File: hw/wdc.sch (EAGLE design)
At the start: 14 parts

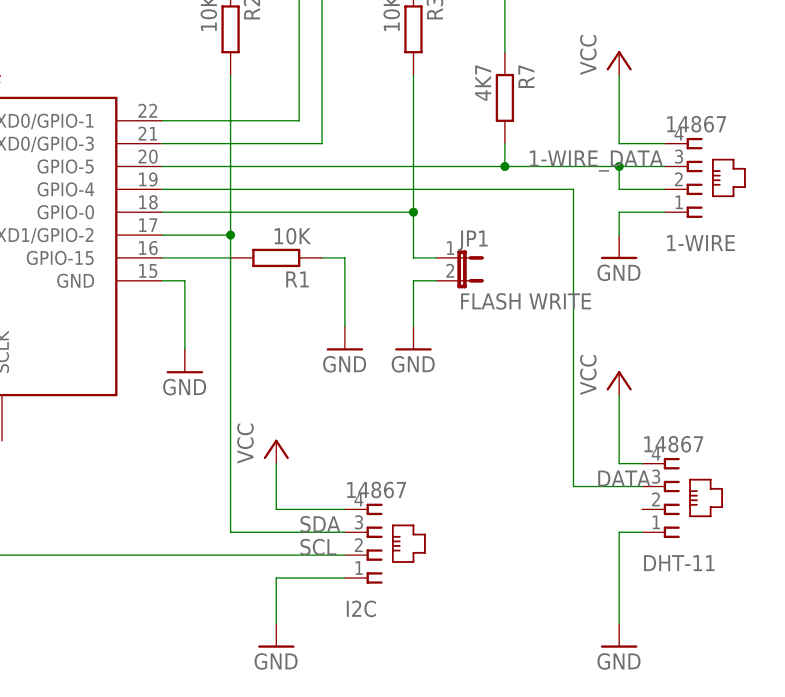
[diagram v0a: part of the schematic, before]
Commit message: Add natsCmd.js to send commands to the sensors through NATS Add wds.js to subscribe and log messages sent by the sensors through NATS Set temp sensor resolution during startup Change NATS server config to point nano pi neo
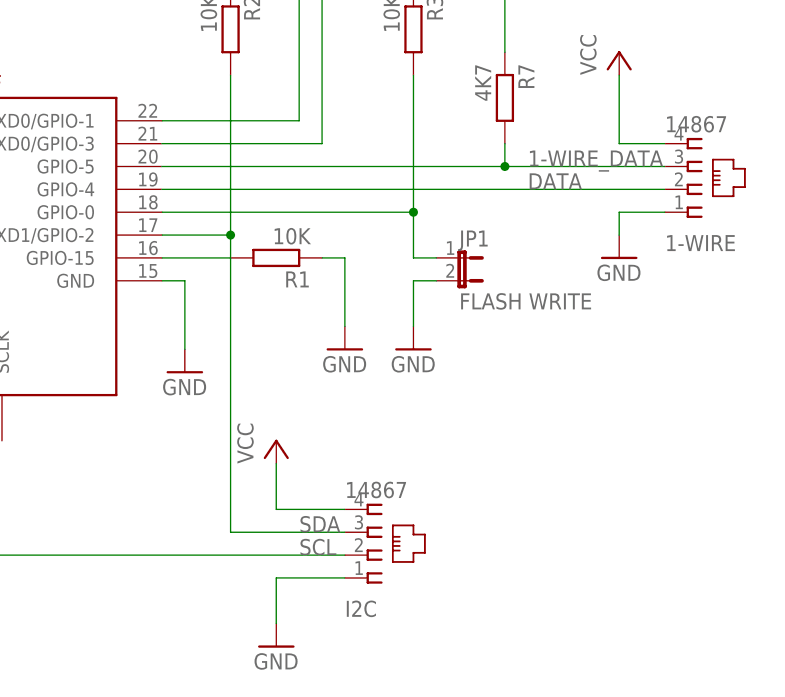
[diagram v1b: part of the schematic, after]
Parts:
- removed DHT-11: 14867, con-4ucon:14867
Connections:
- net 1-WIRE_DATA: no longer 1-WIRE.2
- net DATA: now also 1-WIRE.2; no longer DHT-11.3
- net GND: no longer DHT-11.1
- net VCC: no longer DHT-11.4
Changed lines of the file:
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@@
 <part name="GND5" library="supply1" deviceset="GND" device=""/>
 <part name="P+6" library="supply1" deviceset="VCC" device=""/>
-<part name="P+7" library="supply1" deviceset="VCC" device=""/>
-<part name="GND6" library="supply1" deviceset="GND" device=""/>
 <part name="GND7" library="supply1" deviceset="GND" device=""/>
 <part name="P+8" library="supply1" deviceset="VCC" device=""/>
@@
 <part name="GND13" library="supply1" deviceset="GND" device=""/>
 <part name="1-WIRE" library="con-4ucon" deviceset="14867" device=""/>
-<part name="DHT-11" library="con-4ucon" deviceset="14867" device=""/>
 <part name="I2C" library="con-4ucon" deviceset="14867" device=""/>
 </parts>
@@
 <instance part="GND5" gate="1" x="68.58" y="-60.96"/>
 <instance part="P+6" gate="VCC" x="68.58" y="-38.1"/>
-<instance part="P+7" gate="VCC" x="106.68" y="-30.48"/>
-<instance part="GND6" gate="1" x="106.68" y="-60.96"/>
 <instance part="GND7" gate="1" x="106.68" y="-17.78"/>
 <instance part="P+8" gate="VCC" x="106.68" y="5.08"/>
@@
 <instance part="GND13" gate="1" x="78.74" y="30.48"/>
 <instance part="1-WIRE" gate="G$1" x="114.3" y="-7.62" rot="MR180"/>
-<instance part="DHT-11" gate="G$1" x="111.76" y="-43.18" rot="MR180"/>
 <instance part="I2C" gate="G$1" x="78.74" y="-48.26" rot="MR180"/>
 </instances>
@@
 <wire x1="68.58" y1="-45.72" x2="68.58" y2="-40.64" width="0.1524" layer="91"/>
 </segment>
-<segment>
-<pinref part="DHT-11" gate="G$1" pin="4"/>
-<pinref part="P+7" gate="VCC" pin="VCC"/>
-<wire x1="109.22" y1="-40.64" x2="106.68" y2="-40.64" width="0.1524" layer="91"/>
-<wire x1="106.68" y1="-40.64" x2="106.68" y2="-33.02" width="0.1524" layer="91"/>
-</segment>
 </net>
 <net name="GND" class="0">
@@
 <wire x1="68.58" y1="-53.34" x2="68.58" y2="-58.42" width="0.1524" layer="91"/>
 </segment>
-<segment>
-<pinref part="DHT-11" gate="G$1" pin="1"/>
-<pinref part="GND6" gate="1" pin="GND"/>
-<wire x1="109.22" y1="-48.26" x2="106.68" y2="-48.26" width="0.1524" layer="91"/>
-<wire x1="106.68" y1="-48.26" x2="106.68" y2="-58.42" width="0.1524" layer="91"/>
-</segment>
 </net>
 <net name="N$3" class="0">
@@
 <net name="DATA" class="0">
 <segment>
-<wire x1="109.22" y1="-43.18" x2="101.6" y2="-43.18" width="0.1524" layer="91"/>
-<wire x1="101.6" y1="-43.18" x2="101.6" y2="-10.16" width="0.1524" layer="91"/>
 <pinref part="U$1" gate="G$1" pin="GPIO-4"/>
-<wire x1="101.6" y1="-10.16" x2="55.88" y2="-10.16" width="0.1524" layer="91"/>
-<pinref part="DHT-11" gate="G$1" pin="3"/>
-<label x="104.14" y="-43.18" size="1.778" layer="95"/>
+<wire x1="111.76" y1="-10.16" x2="55.88" y2="-10.16" width="0.1524" layer="91"/>
+<label x="96.52" y="-10.16" size="1.778" layer="95"/>
+<pinref part="1-WIRE" gate="G$1" pin="2"/>
 </segment>
 </net>
@@
 <wire x1="55.88" y1="-7.62" x2="93.98" y2="-7.62" width="0.1524" layer="91"/>
 <label x="96.52" y="-7.62" size="1.778" layer="95"/>
-<wire x1="93.98" y1="-7.62" x2="106.68" y2="-7.62" width="0.1524" layer="91"/>
+<wire x1="93.98" y1="-7.62" x2="111.76" y2="-7.62" width="0.1524" layer="91"/>
 <pinref part="R7" gate="G$1" pin="2"/>
 <wire x1="93.98" y1="-5.08" x2="93.98" y2="-7.62" width="0.1524" layer="91"/>
 <junction x="93.98" y="-7.62"/>
 <pinref part="1-WIRE" gate="G$1" pin="3"/>
-<pinref part="1-WIRE" gate="G$1" pin="2"/>
-<wire x1="106.68" y1="-7.62" x2="111.76" y2="-7.62" width="0.1524" layer="91"/>
-<wire x1="111.76" y1="-10.16" x2="106.68" y2="-10.16" width="0.1524" layer="91"/>
-<wire x1="106.68" y1="-10.16" x2="106.68" y2="-7.62" width="0.1524" layer="91"/>
-<junction x="106.68" y="-7.62"/>
-</segment>
-</net>
+</segment>
+</net>
